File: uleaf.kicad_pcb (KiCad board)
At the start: 4 copper layers, 21.8 x 26.7 mm, 22 parts, among them J3 Conn_01x10, J4 Conn_01x10, U1 STM32G474CCUx, U2 PCM5102, U3 APS6404L-3SQRx-SN, U4 W25Q128JVS, Y1 Crystal_GND24

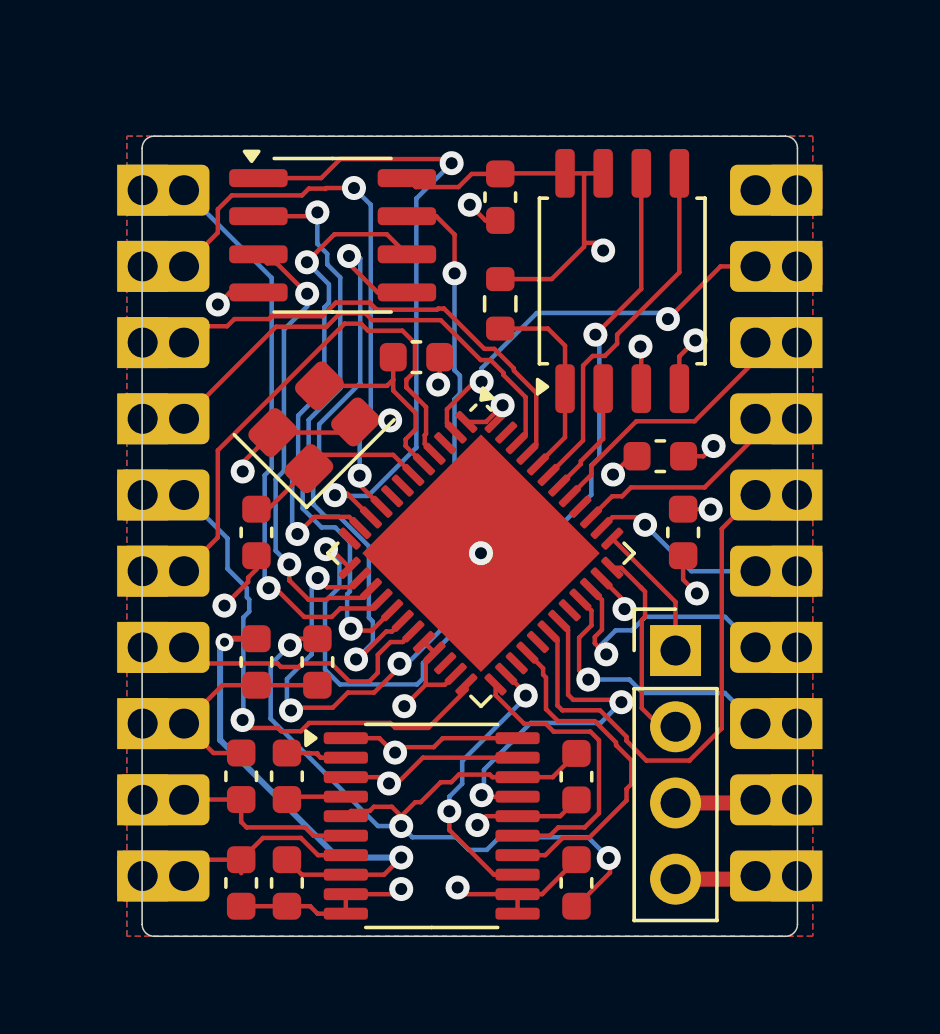
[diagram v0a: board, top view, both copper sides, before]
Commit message: Fixed problem with VNEG pin
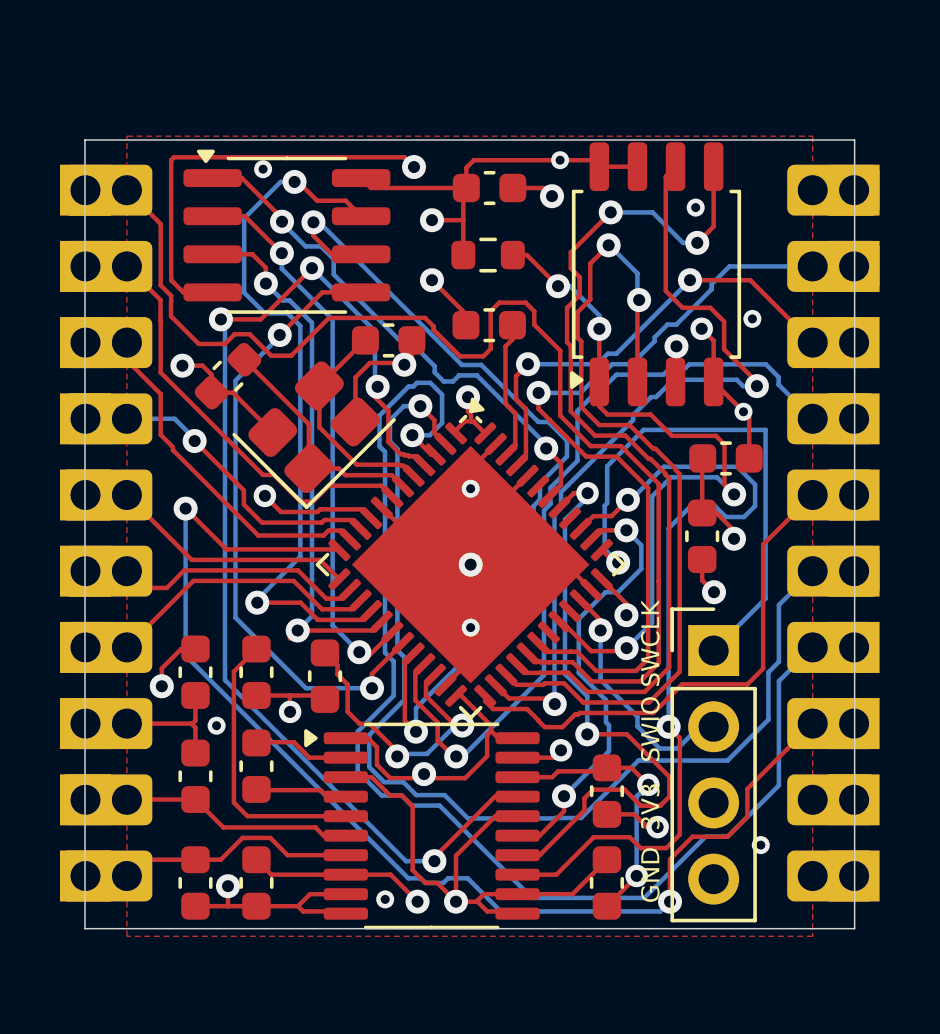
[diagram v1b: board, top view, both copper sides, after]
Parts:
- removed U1: STM32G474CCUx, Package_DFN_QFN:QFN-48-1EP_7x7mm_P0.5mm_EP5.6x5.6mm
- added C7: 2.2u, Capacitor_SMD:C_0603_1608Metric, F.Cu at (150.5, 82.5)
- added C8: 2.2u, Capacitor_SMD:C_0603_1608Metric, F.Cu at (145.0, 94.2)
- added U5: STM32H533CEUx, Package_DFN_QFN:QFN-48-1EP_7x7mm_P0.5mm_EP5.6x5.6mm, F.Cu at (149.9, 90.5)
- J3, J4: footprint uleaf:PinHeader_1x10_P2.54mm_Vertical -> uleaf:PinHeader_1x10_P2.54mm_Vertical_Castellated
- moved C17 5.29 mm to (141.8, 84.2), turned to 45 degrees
- moved C10 2.19 mm to (158.4, 86.9)
- moved C3 2.06 mm to (142.7, 94.1)
- moved C9 2.06 mm to (140.7, 94.1)
- moved J3 1.91 mm to (138.4, 100.9)
- moved J4 1.91 mm to (161.3, 78.0)
- moved R1 1.68 mm to (150.5, 80.2), turned to 0 degrees
- moved C5 1.52 mm to (140.7, 101.1)
- moved C6 1.52 mm to (140.7, 97.5)
- moved U3 1.52 mm to (143.8, 79.5)
- moved J2 1.27 mm to (158.0, 93.3)
- moved U4 1.16 mm to (156.1, 80.8)
- moved C2 1.12 mm to (154.4, 98.0)
- moved C16 1.08 mm to (147.2, 83.0)
- moved C1 1.07 mm to (142.7, 97.2)
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- renumbered SWDCLK to J2
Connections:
- net /SPI1_CS renamed /SPI2_CS
- C3 pad 2: Net-(U2-LDOO) -> Net-(U2-VNEG)
- J3 pad 10: /I2C2_SCL -> /PA8
- J3 pad 4: /GPIO_PB2 -> /PA5
- J3 pad 5: /GPIO_PC15 -> /PA4
- J3 pad 6: /ADC4_IN14 -> /PA3
- J3 pad 7: /I2C1_SCL -> /PA0
- J3 pad 8: /I2C1_SDA -> /PA1
- J3 pad 9: /ADC2_IN2 -> /NRST
- J4 pad 2: /GPIO_PC13 -> /PA9
- J4 pad 3: /TIM2_CH2 -> /PB8
- J4 pad 4: /GPIO_PC10 -> /PB10
- J4 pad 5: /I2C2_SDA -> /PB12
- J4 pad 6: /TIM2_CH1 -> /PC13
- J4 pad 7: /TIM4_CH2 -> /PC14
- J4 pad 8: /TIM4_CH1 -> /PA2
- U2 pad 13: /I2S2_CK -> /I2S1_CK
- U2 pad 14: /I2S2_SD -> /I2S1_SD
- U2 pad 15: /I2S2_WS -> /I2S1_WS
- U2 pad 5: Net-(U2-LDOO) -> Net-(U2-VNEG)
- U4 pad 2: /SPI1_MISO -> /SPI2_MISO
- U4 pad 5: /SPI1_MOSI -> /SPI2_MOSI
- U4 pad 6: /SPI1_SCK -> /SPI2_SCK
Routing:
- net /PC14: track 0.00 -> 40.8 mm, vias 0 -> 1
- net /PA8: track 0.00 -> 39.5 mm
- net /PA2: track 0.00 -> 39.1 mm, vias 0 -> 2
- net /PC13: track 0.00 -> 36.0 mm, vias 0 -> 1
- net GND: track 53.9 -> 88.5 mm, vias 14 -> 22
- net /SPI2_MOSI: track 0.00 -> 29.9 mm, vias 0 -> 2
- net /SPI1_SCK: track 29.0 -> 0.00 mm, vias 2 -> 0
- net /SPI2_MISO: track 0.00 -> 28.3 mm, vias 0 -> 2
- net /I2S1_CK: track 0.00 -> 27.8 mm, vias 0 -> 2
- net /SPI2_SCK: track 0.00 -> 26.9 mm, vias 0 -> 2
- net /PB10: track 0.00 -> 26.5 mm, vias 0 -> 1
- net /PA9: track 0.00 -> 26.2 mm, vias 0 -> 1
- net /PCM_MUTE_CONTROL: track 12.1 -> 37.6 mm, vias 2 -> 4
- net /I2S1_SD: track 0.00 -> 20.3 mm, vias 0 -> 2
- net Net-(U2-LDOO): track 28.6 -> 9.34 mm, vias 3 -> 2
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- removed copper zone on B.Cu, net GND
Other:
- board size 21.8 x 26.7 mm -> 25.7 x 26.3 mm
- board text added: "NRST"
- board text added: "PA0"
- board text added: "PA2"
- board text added: "PA3"
- board text added: "PA4"
- board text added: "PA5"
- board text added: "PA9"
- board text added: "PB10"
- board text added: "PB12"
- board text added: "PC14"
- board text added: "SWCLK"
- board text added: "SWIO"
- board text added: "uLEAF rev 0.2"
- board text removed: "PA11"
- board text removed: "PA12"
- board text removed: "PA15"
- board text removed: "PB11"
- board text removed: "PB2"
- board text removed: "PB3"
- board text removed: "PB7"
- board text removed: "PC10"
- board text removed: "PC15"
- board text removed: "PC4"
- board text removed: "uLEAF rev 0.1"

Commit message: Fixed problem with output DAC output filters
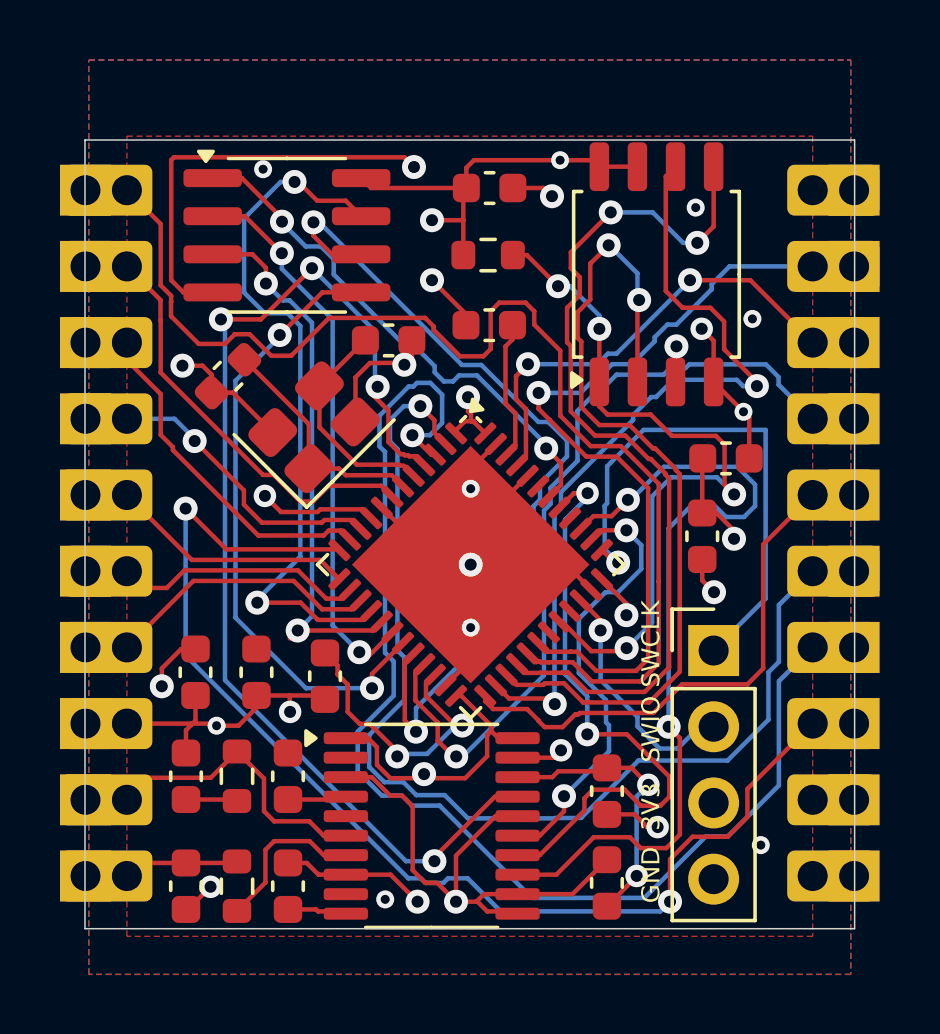
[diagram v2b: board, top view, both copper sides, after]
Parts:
- added R2: 470, Resistor_SMD:R_0603_1608Metric, F.Cu at (142.1, 97.5)
- added R3: 470, Resistor_SMD:R_0603_1608Metric, F.Cu at (142.1, 101.2)
- C5, C6: value 2.2u -> 2.2nF
- moved C1 1.10 mm to (143.8, 97.5)
- moved C14 1.06 mm to (143.8, 101.2)
- moved C5 0.33 mm to (140.4, 101.2)
- moved C6 0.32 mm to (140.4, 97.5)
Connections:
- C6 pad 2: /OUT_L -> Net-(C6-Pad2)
- U2 pad 7: /OUT_R -> Net-(U2-OUTR)
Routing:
- net Net-(U2-VNEG): track 9.35 -> 0.00 mm
- net Net-(U2-OUTR): track 0.00 -> 5.52 mm
- net /OUT_R: track 8.06 -> 4.64 mm
- net Net-(U2-CAPP): track 3.20 -> 0.00 mm
- net /OUT_L: track 7.80 -> 9.76 mm
- net Net-(C6-Pad2): track 0.00 -> 1.72 mm
- net GND: track 88.5 -> 86.9 mm
- net +3.3V: track 43.4 -> 42.3 mm
- added copper zone on B.Cu, net GND
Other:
- board text added: "uLEAF rev 0.3"
- board text removed: "uLEAF rev 0.2"
